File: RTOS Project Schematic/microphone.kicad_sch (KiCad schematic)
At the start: 2 parts

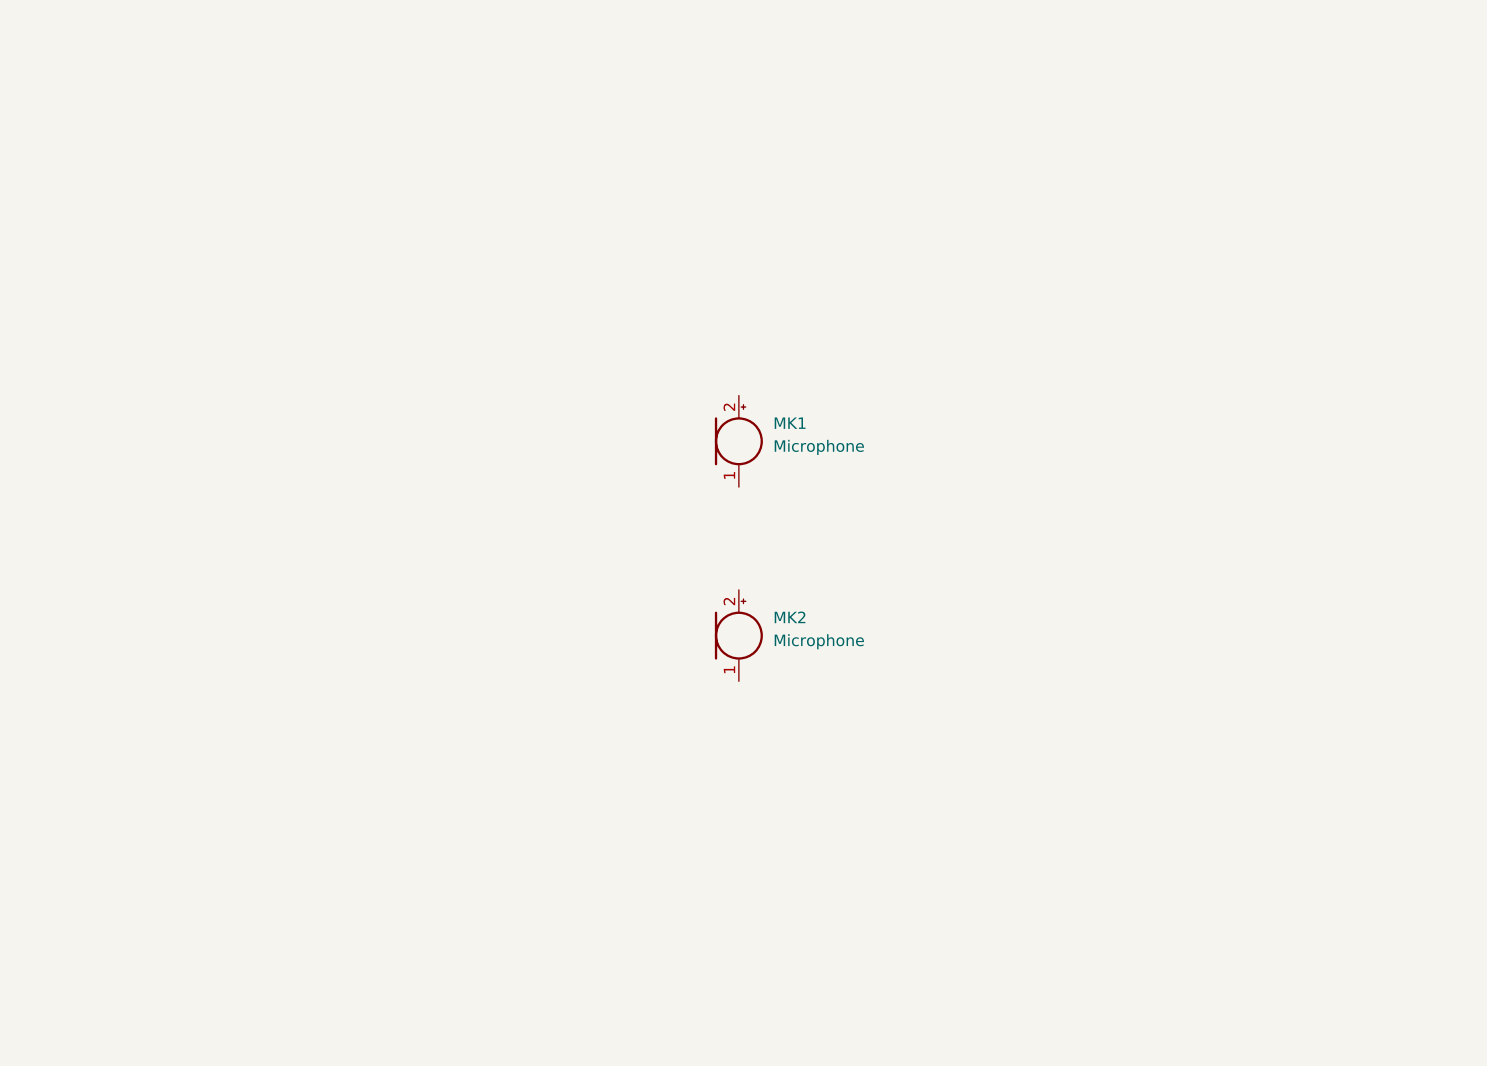
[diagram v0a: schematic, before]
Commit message: Added preliminary microphone circuit
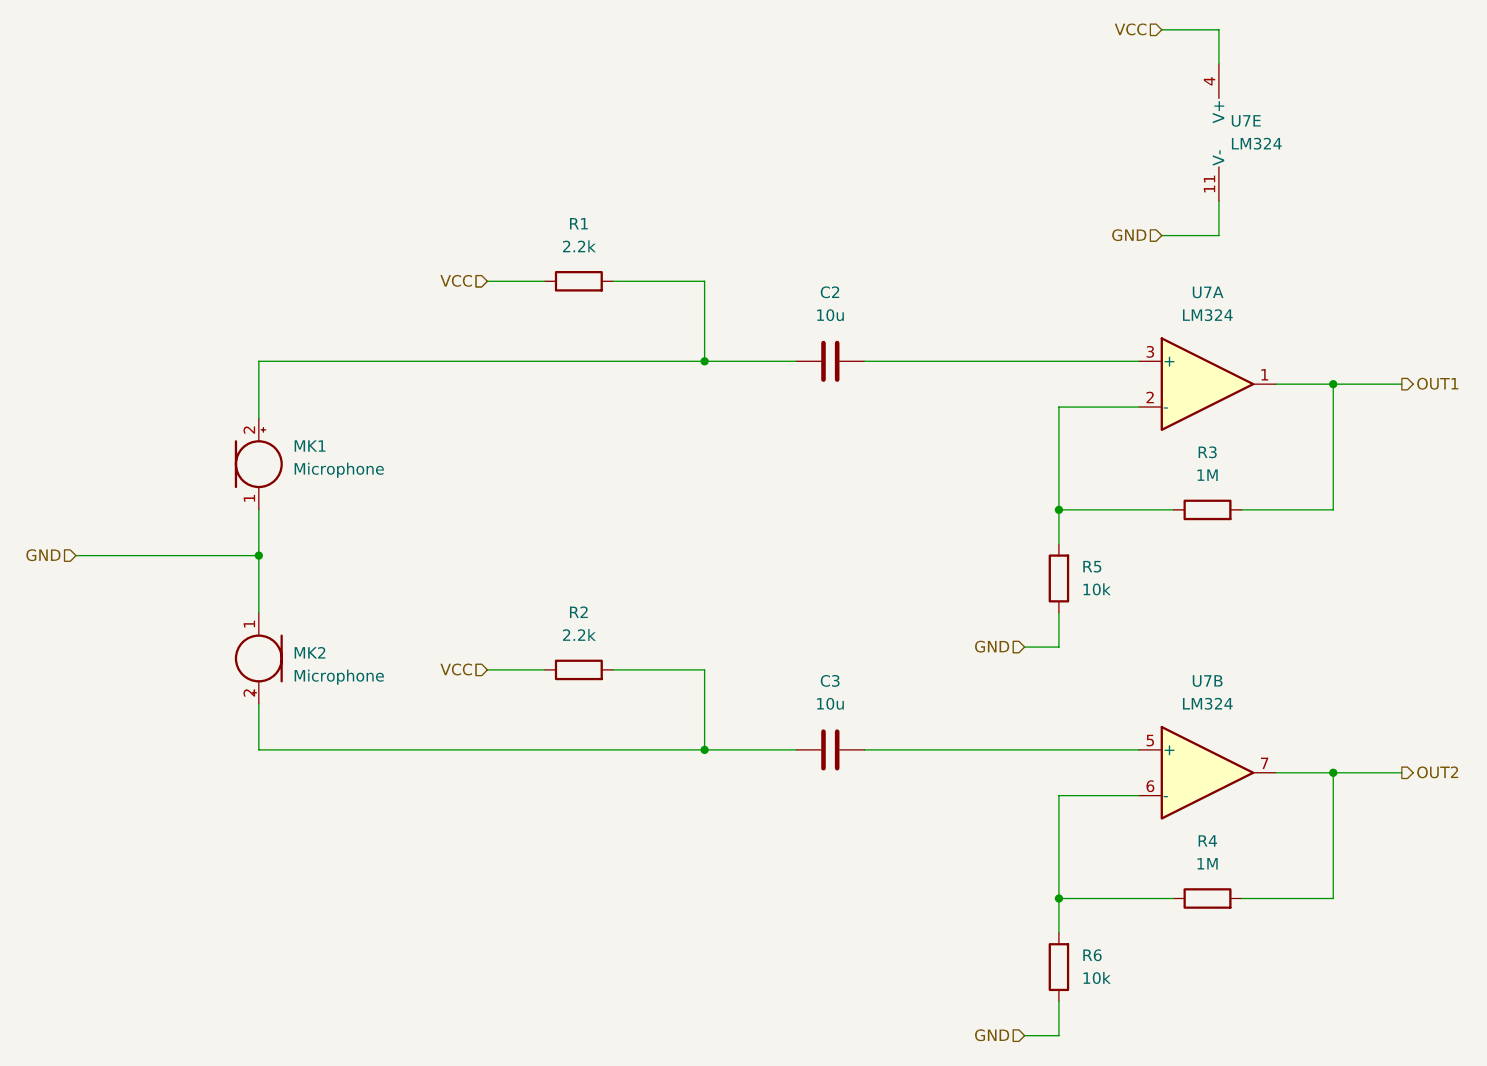
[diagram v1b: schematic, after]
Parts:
- added C2, C3: 10u, symbol Device:C
- added R1, R2: 2.2k, symbol Device:R
- added R3, R4: 1M, symbol Device:R
- added R5, R6: 10k, symbol Device:R
- added U7: LM324, symbol Amplifier_Operational:LM324
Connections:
- net GND: now reaches MK2.1 (-)
- net GND: now also MK1.1 (-), R5.1, R6.1, U7.11 (V-)
- net at MK2.2 (+): now also C3.1, R2.2
- net at MK1.2 (+): now also C2.1, R1.2
- new net: R4.1, R6.2, U7.6 (-)
- new net: R3.1, R5.2, U7.2 (-)
- new net: C2.2, U7.3 (+)
- new net: C3.2, U7.5 (+)
- new net OUT1: R3.2, U7.1
- new net OUT2: R4.2, U7.7
- new net VCC: R1.1, R2.1, U7.4 (V+)
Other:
- company: (none) -> Eddie and Felix
- title: (none) -> Microphones
- moved on the sheet: MK1, MK2
